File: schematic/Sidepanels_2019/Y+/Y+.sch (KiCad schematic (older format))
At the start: 42 parts, among them J1 Conn_01x04, J2 Conn_01x02

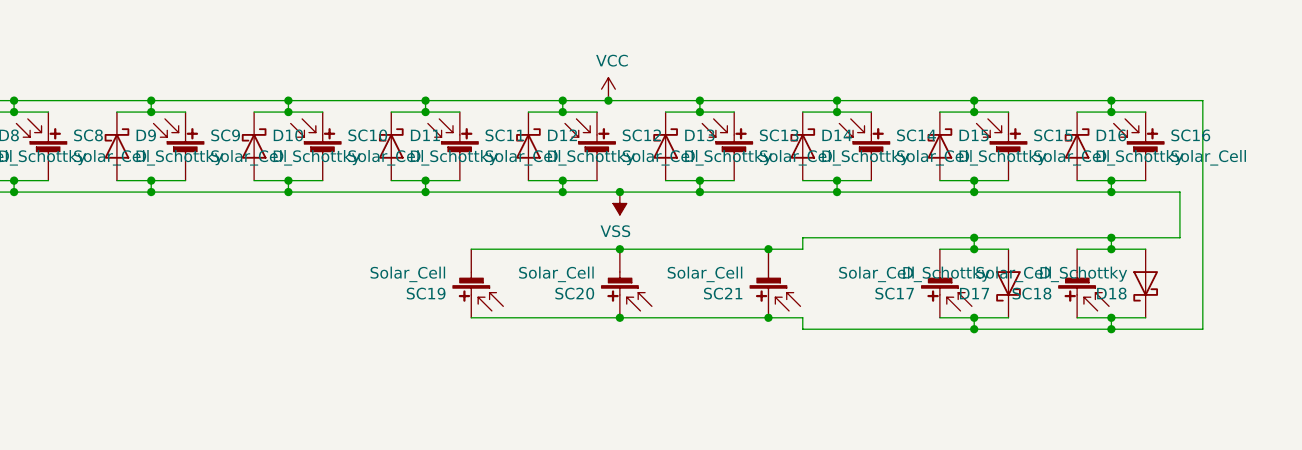
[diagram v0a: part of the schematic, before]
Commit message: Flipped and/or added TrisolX cells
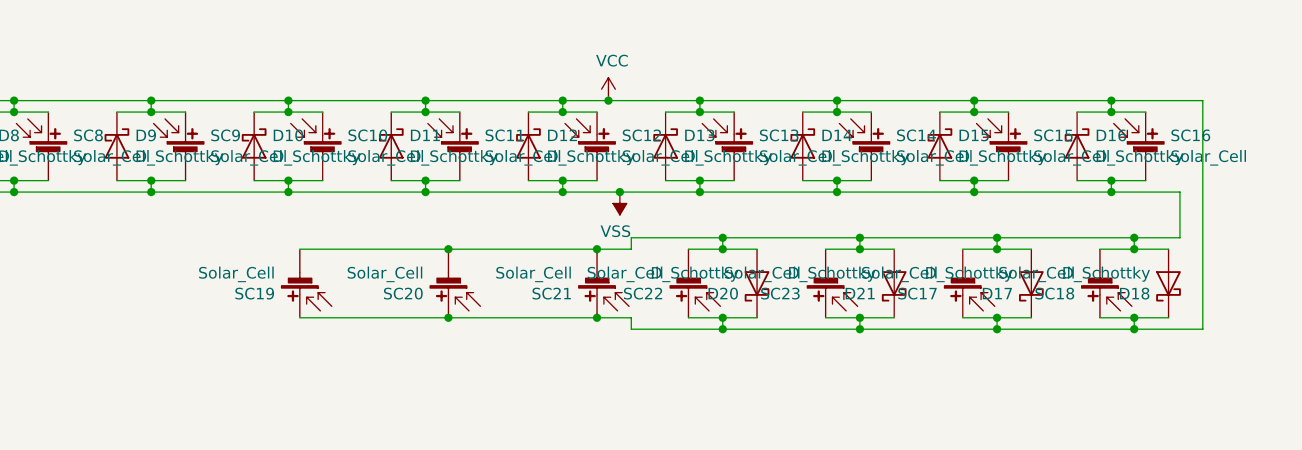
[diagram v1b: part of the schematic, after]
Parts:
- added D20, D21: D_Schottky, CySat footprints:Toshiba_CUS08F30, symbol Device:D_Schottky
- added SC22, SC23: Solar_Cell, CySat footprints:TriSelectSolarPanel_Left_Handed, symbol Device:Solar_Cell
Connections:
- net VCC: now also D20.1 (K), D21.1 (K), SC22.1 (+), SC23.1 (+)
- net VSS: now also D20.2 (A), D21.2 (A), SC22.2 (-), SC23.2 (-)
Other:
- moved on the sheet: D17, D18, SC17, SC18, SC19, SC20, SC21

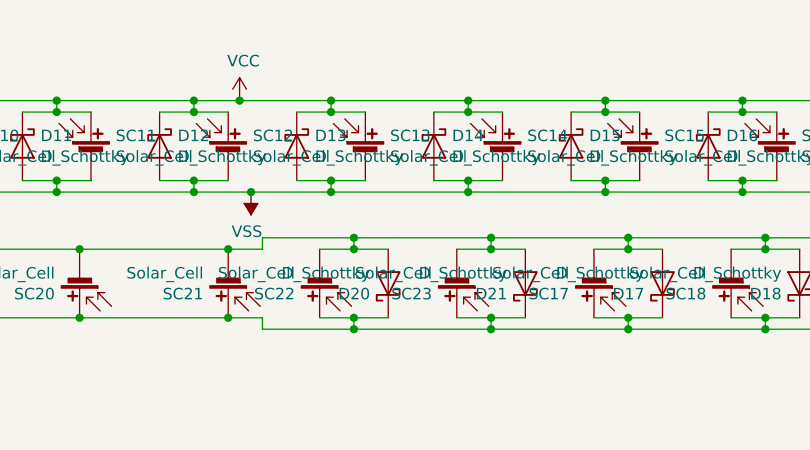
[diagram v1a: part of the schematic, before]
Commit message: Fixed Trisol Cells
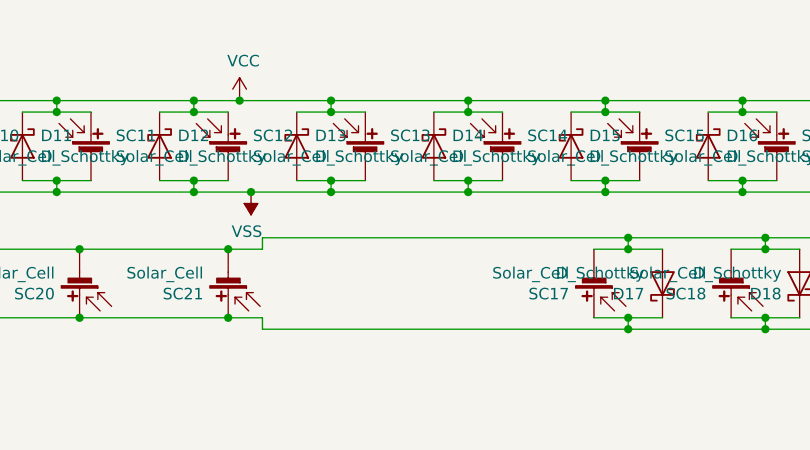
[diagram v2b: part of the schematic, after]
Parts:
- removed D20, D21: D_Schottky, CySat footprints:Toshiba_CUS08F30, symbol Device:D_Schottky
- removed SC22, SC23: Solar_Cell, CySat footprints:TriSelectSolarPanel_Left_Handed, symbol Device:Solar_Cell
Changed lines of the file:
@@
 	6250 3950 6900 3950
 Connection ~ 9300 3600
-Connection ~ 9300 4000
 Connection ~ 9900 3600
 Connection ~ 9900 4000
@@
 Wire Wire Line
 	9300 4000 9900 4000
-$Comp
-L Device:D_Schottky D21
-U 1 1 5D911955
-P 8850 3800
-F 0 "D21" V 8804 3879 50  0000 L CNN
-F 1 "D_Schottky" V 8895 3879 50  0000 L CNN
-F 2 "CySat footprints:Toshiba_CUS08F30" H 8850 3800 50  0001 C CNN
-F 3 "~" H 8850 3800 50  0001 C CNN
-	1    8850 3800
-	0    -1   -1   0
-$EndComp
-$Comp
-L Device:Solar_Cell SC23
-U 1 1 5D91195F
-P 8550 3750
-F 0 "SC23" H 8658 3846 50  0000 L CNN
-F 1 "Solar_Cell" H 8658 3755 50  0000 L CNN
-F 2 "CySat footprints:TriSelectSolarPanel_Left_Handed" V 8550 3810 50  0001 C CNN
-F 3 "~" V 8550 3810 50  0001 C CNN
-	1    8550 3750
-	-1   0    0    1
-$EndComp
 Wire Wire Line
-	8850 3650 8700 3650
+	7700 3600 9300 3600
 Wire Wire Line
-	8850 3950 8700 3950
-Wire Wire Line
-	8700 3950 8700 4000
-Connection ~ 8700 3950
-Wire Wire Line
-	8700 3950 8550 3950
-Wire Wire Line
-	8700 3650 8700 3600
-Connection ~ 8700 3650
-Wire Wire Line
-	8700 3650 8550 3650
-$Comp
-L Device:D_Schottky D20
-U 1 1 5D911971
-P 8250 3800
-F 0 "D20" V 8204 3879 50  0000 L CNN
-F 1 "D_Schottky" V 8295 3879 50  0000 L CNN
-F 2 "CySat footprints:Toshiba_CUS08F30" H 8250 3800 50  0001 C CNN
-F 3 "~" H 8250 3800 50  0001 C CNN
-	1    8250 3800
-	0    -1   -1   0
-$EndComp
-$Comp
-L Device:Solar_Cell SC22
-U 1 1 5D91197B
-P 7950 3750
-F 0 "SC22" H 8058 3846 50  0000 L CNN
-F 1 "Solar_Cell" H 8058 3755 50  0000 L CNN
-F 2 "CySat footprints:TriSelectSolarPanel_Left_Handed" V 7950 3810 50  0001 C CNN
-F 3 "~" V 7950 3810 50  0001 C CNN
-	1    7950 3750
-	-1   0    0    1
-$EndComp
-Wire Wire Line
-	8250 3650 8100 3650
-Wire Wire Line
-	8250 3950 8100 3950
-Wire Wire Line
-	8100 3950 8100 4000
-Connection ~ 8100 3950
-Wire Wire Line
-	8100 3950 7950 3950
-Wire Wire Line
-	8100 3650 8100 3600
-Connection ~ 8100 3650
-Wire Wire Line
-	8100 3650 7950 3650
-Connection ~ 8700 3600
-Wire Wire Line
-	8700 3600 9300 3600
-Connection ~ 8700 4000
-Wire Wire Line
-	8700 4000 9300 4000
-Wire Wire Line
-	7700 3600 8100 3600
-Connection ~ 8100 3600
-Wire Wire Line
-	8100 3600 8700 3600
-Wire Wire Line
-	7700 4000 8100 4000
-Connection ~ 8100 4000
-Wire Wire Line
-	8100 4000 8700 4000
+	9300 4000 7700 4000
+Connection ~ 9300 4000
 $EndSCHEMATC

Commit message: Update to Y+
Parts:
- removed D1, D10, D11, D12, D13, D14, D15, D16, D17, D18, D2, D3, D4, D5, D6, D7, D8, D9: D_Schottky, CySat footprints:Toshiba_CUS08F30, symbol Device:D_Schottky
- removed SC1, SC10, SC11, SC12, SC13, SC14, SC15, SC16, SC17, SC18, SC2, SC3, SC5, SC6, SC7, SC8, SC9: Solar_Cell, CySat footprints:TriSelectSolarPanel, symbol Device:Solar_Cell
- D1: renamed from D19; footprint CySat footprints:Sun_Sensor -> Diode_SMD:D_0805_2012Metric
- SC1: renamed from SC19; footprint CySat footprints:Spectrolab -> CySat_Solar:Spectrolab
- SC2: renamed from SC20; footprint CySat footprints:Spectrolab -> CySat_Solar:Spectrolab
- SC3: renamed from SC21; footprint CySat footprints:Spectrolab -> CySat_Solar:Spectrolab
- SC4: footprint CySat footprints:TriSelectSolarPanel -> CySat_Solar:Spectrolab
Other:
- moved on the sheet: SC1, SC2, SC3
